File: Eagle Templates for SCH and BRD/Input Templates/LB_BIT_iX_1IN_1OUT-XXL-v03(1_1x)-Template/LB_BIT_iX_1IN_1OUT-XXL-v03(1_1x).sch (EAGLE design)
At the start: 16 parts, among them U1 LV321SOT23-5, U2 LV321SOT23-5

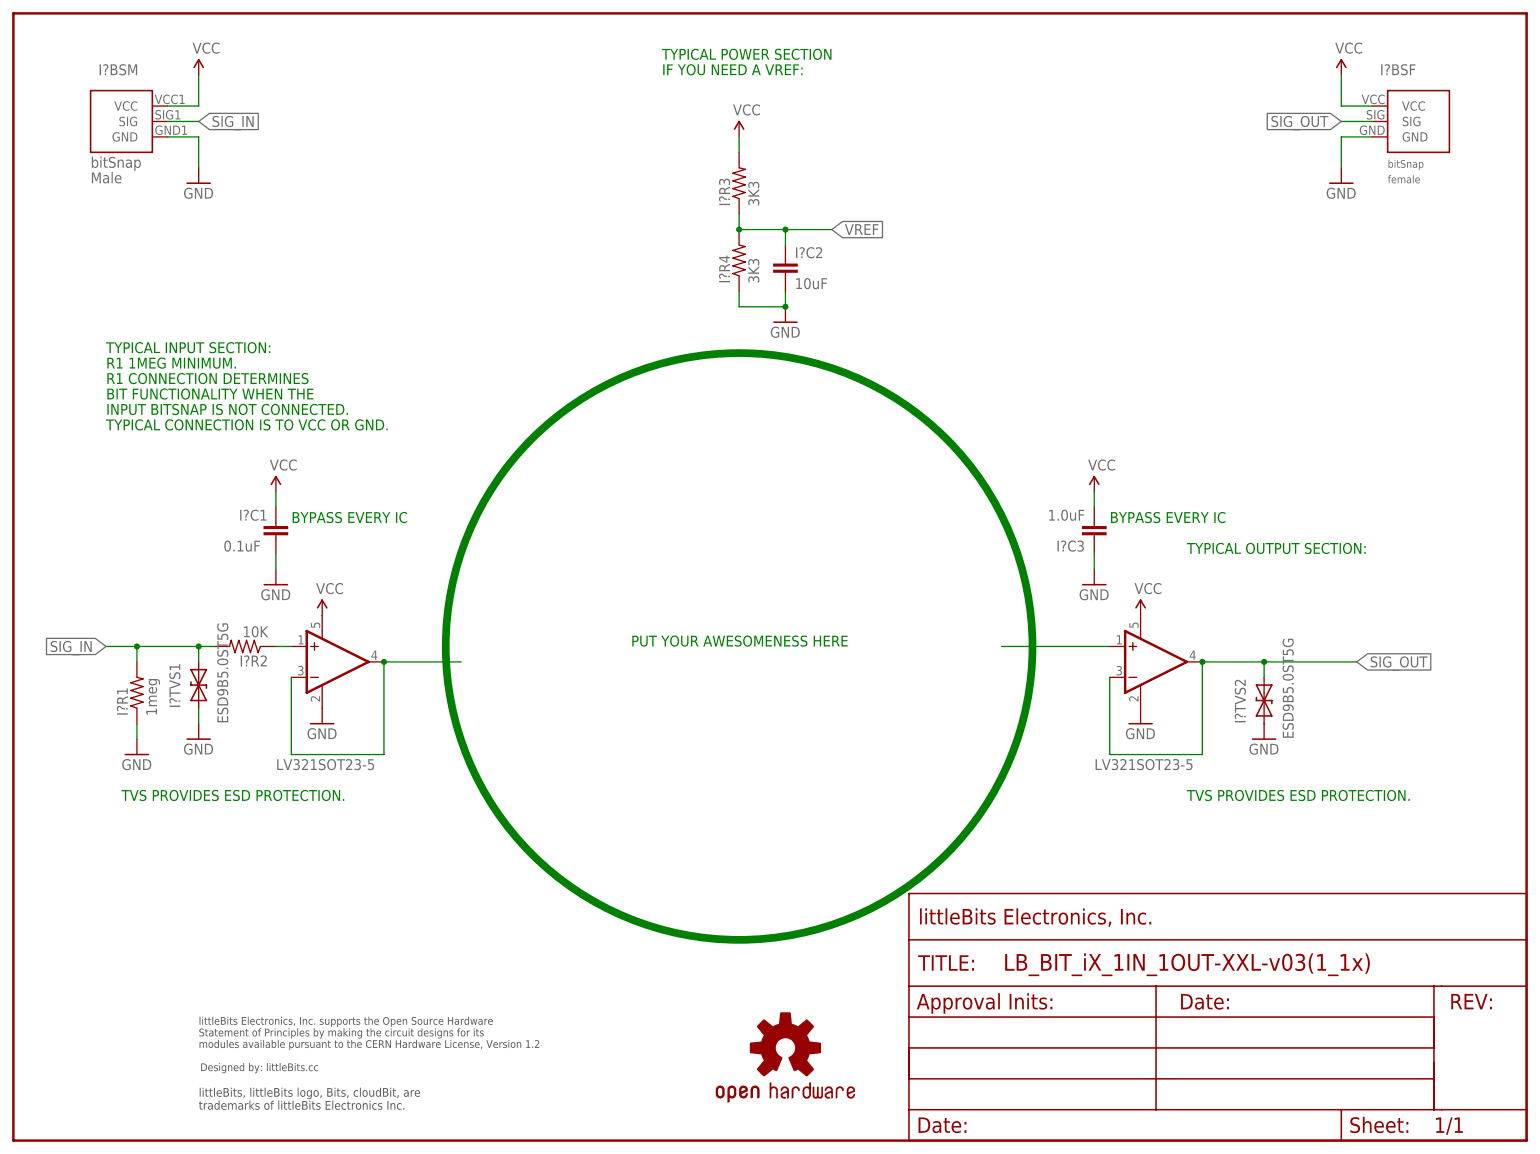
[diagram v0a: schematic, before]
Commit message: Updated templates
- Added ferrite beads
- Moved text and annotations off of Nets layer
- Minor layout changes
- Removed I/O/W prefix from reference designators
- Removed output stage components from output bits
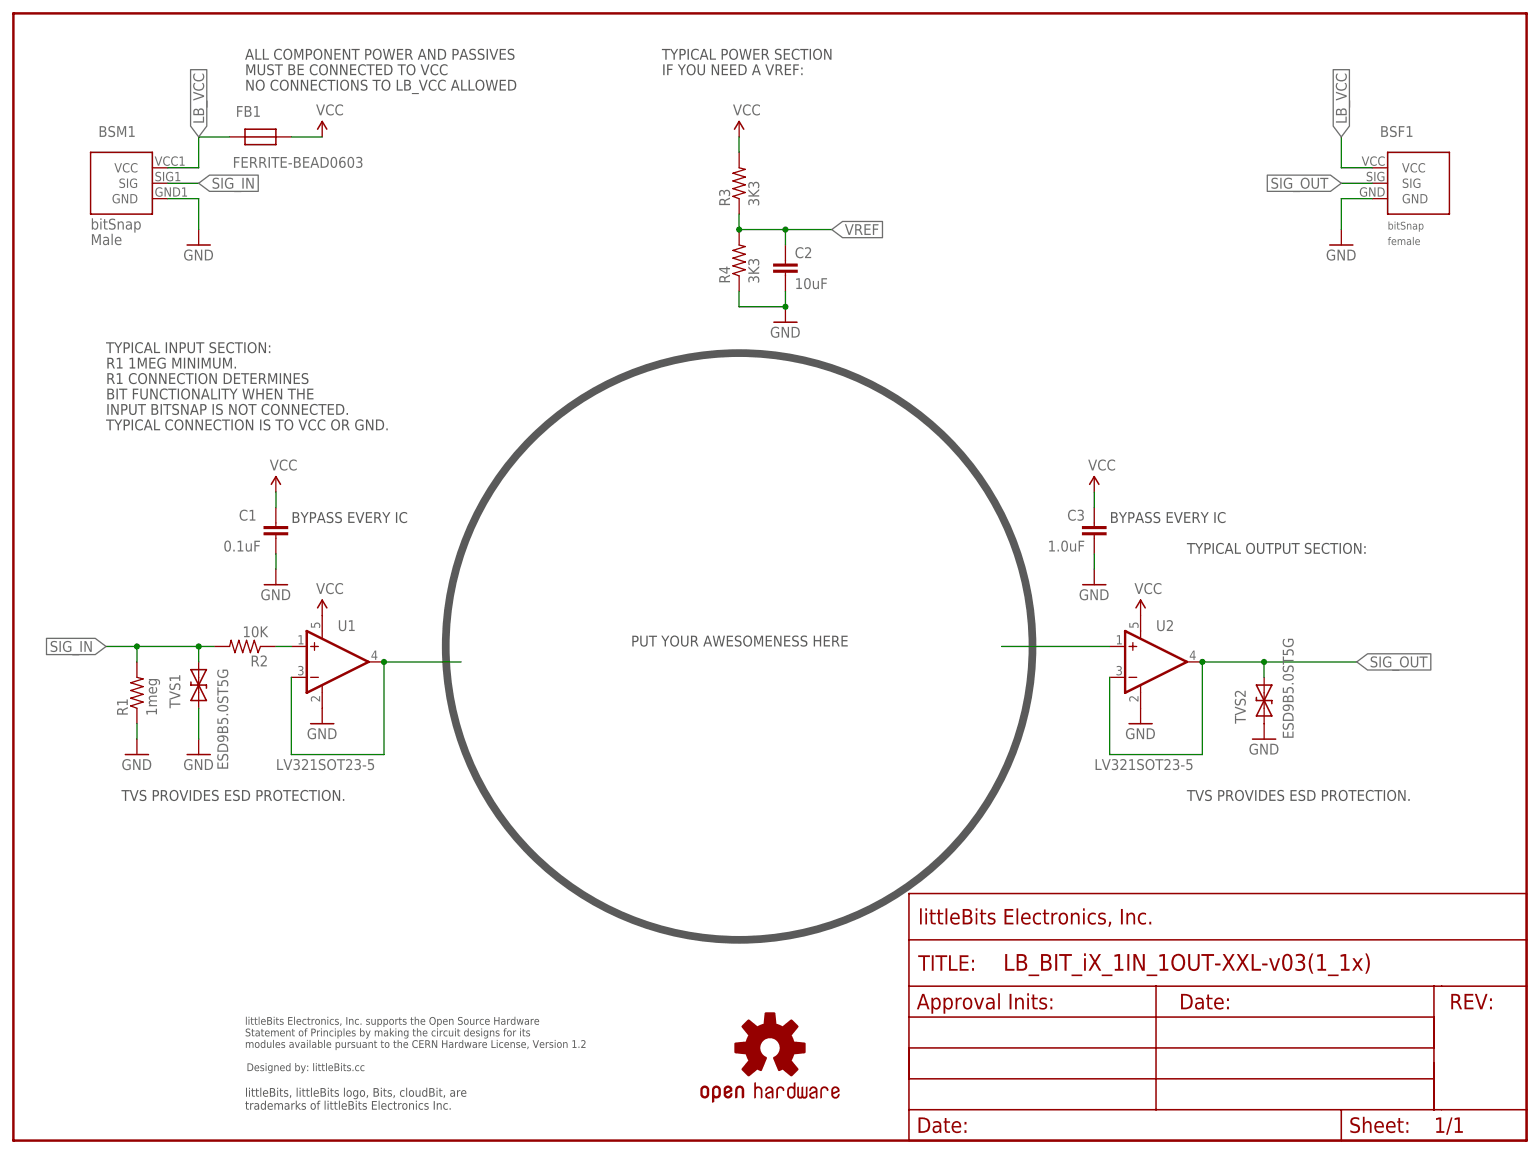
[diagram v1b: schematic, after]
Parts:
- removed I?BSF: BITSNAP_V03_FEMALE, bitSnap:BITSNAP_V03_FEMALE
- removed I?BSM: BITSNAP_V03_MALE, bitSnap:BITSNAP_V03_MALE
- added BSF1: BITSNAP_V03_FEMALE, bitSnap:BITSNAP_V03_FEMALE
- added BSM1: BITSNAP_V03_MALE, bitSnap:BITSNAP_V03_MALE
- added FB1: FERRITE-BEAD0603, LITTLEBITS:FERRITE-BEAD0603
- U$1: value FRAME-LETTER -> OSHW-LOGOL; device LITTLEBITS:FRAME-LETTER -> LITTLEBITS131206:OSHW-LOGOL
- U$2: value OSHW-LOGOL -> OSHWCREDIT; device LITTLEBITS131206:OSHW-LOGOL -> LITTLEBITS:OSHWCREDIT
- U$3: value OSHWCREDIT -> FRAME-LETTER; device LITTLEBITS:OSHWCREDIT -> LITTLEBITS:FRAME-LETTER
- renumbered I?C1 to C1, I?C2 to C2, I?C3 to C3, I?R1 to R1, I?R2 to R2, I?R3 to R3, I?R4 to R4, I?TVS1 to TVS1, I?TVS2 to TVS2
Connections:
- new net LB_VCC: BSF1.VCC, BSM1.VCC, FB1.P$2
- net GND: now also BSF1.GND, BSM1.GND; no longer I?BSF.GND, I?BSM.GND
- net SIG_IN: now also BSM1.SIG; no longer I?BSM.SIG
- net SIG_OUT: now also BSF1.SIG; no longer I?BSF.SIG
- net VCC: now also FB1.P$1; no longer I?BSF.VCC, I?BSM.VCC
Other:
- note added: "ALL COMPONENT POWER AND PASSIVES"
- note added: "MUST BE CONNECTED TO VCC"
- note added: "NO CONNECTIONS TO LB_VCC ALLOWED"
